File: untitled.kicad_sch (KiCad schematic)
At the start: 0 parts

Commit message: updated DacSheet
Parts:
- added IC1: ES9023P, customfootprints:SOIC127P600X175-16N, symbol esp32lib:ES9023P
- added U14: NAU88C22YG, customfootprints:nau88c22, symbol modcaneuro:NAU88C22YG

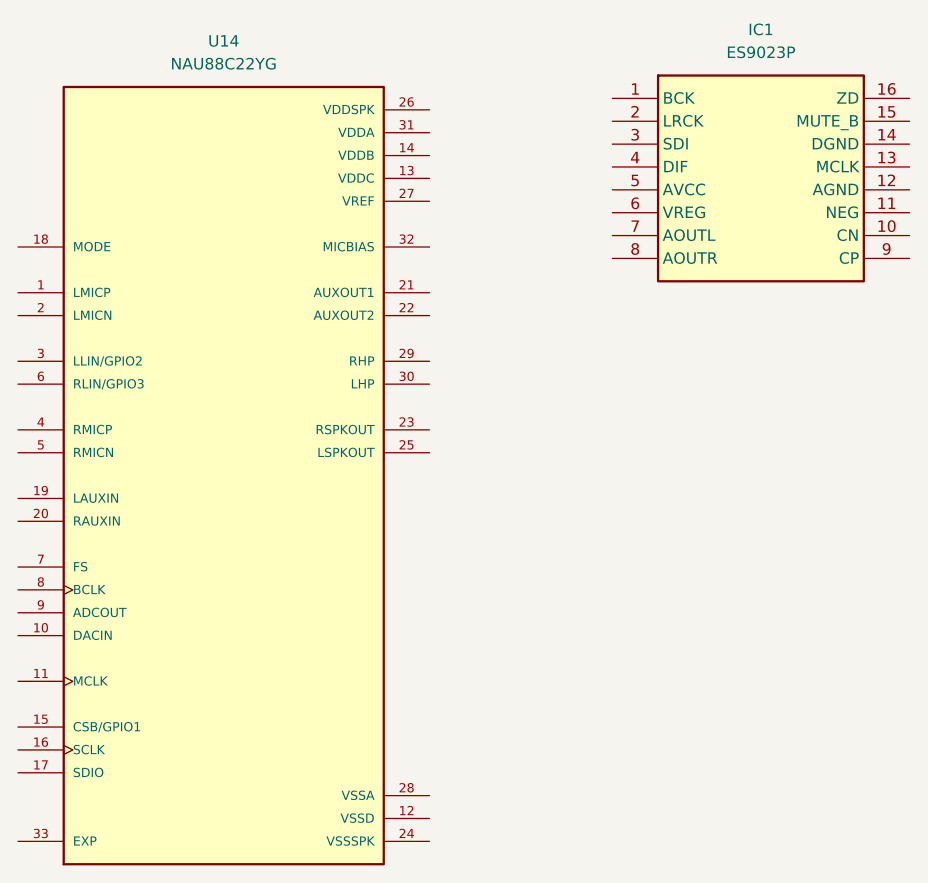
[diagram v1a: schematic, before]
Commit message: added codec
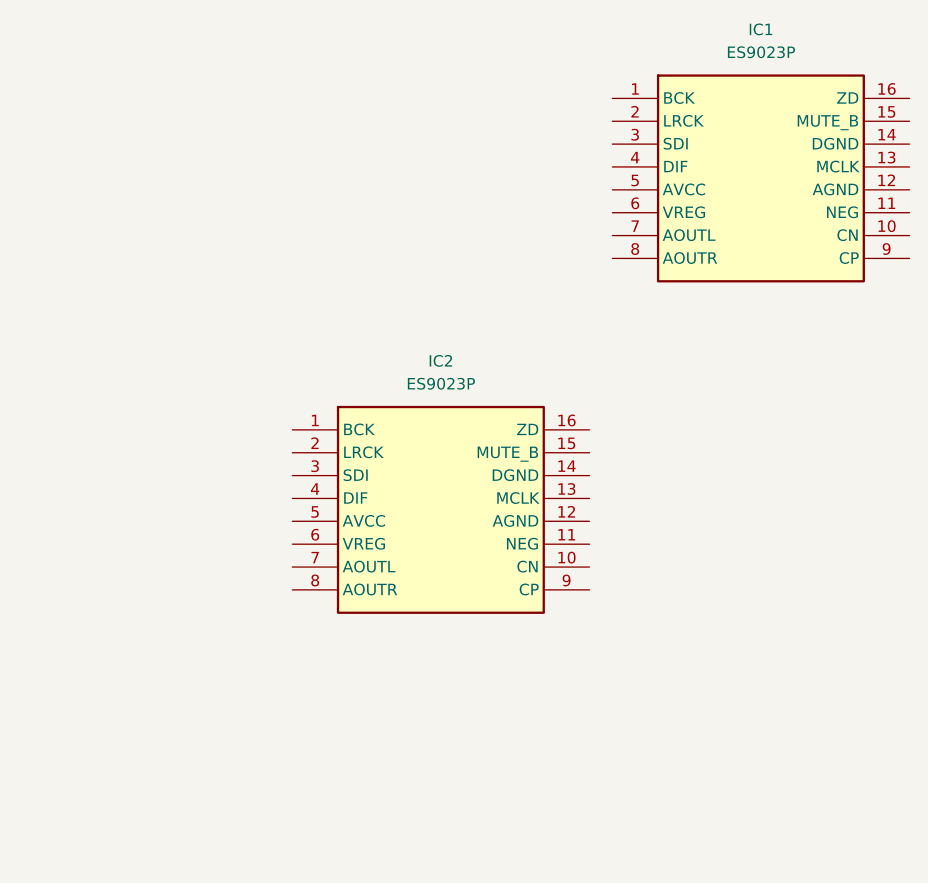
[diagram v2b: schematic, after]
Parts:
- removed U14: NAU88C22YG, customfootprints:nau88c22, symbol modcaneuro:NAU88C22YG
- added IC2: ES9023P, customfootprints:SOIC127P600X175-16N, symbol esp32lib:ES9023P
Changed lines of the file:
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@@
 	)
 	(symbol
-		(lib_id "modcaneuro:NAU88C22YG")
-		(at 163.83 77.47 0)
+		(lib_id "esp32lib:ES9023P")
+		(at 171.45 72.39 0)
 		(unit 1)
 		(exclude_from_sim no)
@@
 		(dnp no)
 		(fields_autoplaced yes)
-		(property "Reference" "U14"
-			(at 163.83 29.21 0)
+		(property "Reference" "IC2"
+			(at 187.96 64.77 0)
 			(effects
 				(font
@@
 			)
 		)
-		(property "Value" "NAU88C22YG"
-			(at 163.83 31.75 0)
+		(property "Value" "ES9023P"
+			(at 187.96 67.31 0)
 			(effects
 				(font
@@
 			)
 		)
-		(property "Footprint" "customfootprints:nau88c22"
-			(at 163.83 77.47 0)
+		(property "Footprint" "customfootprints:SOIC127P600X175-16N"
+			(at 200.66 167.31 0)
 			(effects
 				(font
 					(size 1.27 1.27)
 				)
-				(justify bottom)
+				(justify left top)
 				(hide yes)
 			)
 		)
 		(property "Datasheet" ""
-			(at 163.83 77.47 0)
+			(at 200.66 267.31 0)
+			(effects
+				(font
+					(size 1.27 1.27)
+				)
+				(justify left top)
+				(hide yes)
+			)
+		)
+		(property "Description" "Audio D/A Converter ICs Sabre 2V RMS stereo DAC"
+			(at 171.45 72.39 0)
 			(effects
 				(font
@@
 			)
 		)
-		(property "Description" ""
-			(at 163.83 77.47 0)
+		(property "Height" "1.75"
+			(at 200.66 467.31 0)
 			(effects
 				(font
 					(size 1.27 1.27)
 				)
+				(justify left top)
 				(hide yes)
 			)
 		)
-		(property "PARTREV" "3.3"
-			(at 163.83 77.47 0)
+		(property "Mouser Part Number" "460-ES9023P"
+			(at 200.66 567.31 0)
 			(effects
 				(font
 					(size 1.27 1.27)
 				)
-				(justify bottom)
+				(justify left top)
 				(hide yes)
 			)
 		)
-		(property "STANDARD" "Manufacturer Recommendations"
-			(at 163.83 77.47 0)
+		(property "Mouser Price/Stock" "https://www.mouser.co.uk/ProductDetail/ESS-Technology/ES9023P?qs=sPbYRqrBIVn%252BcPkDS1h3%252BQ%3D%3D"
+			(at 200.66 667.31 0)
 			(effects
 				(font
 					(size 1.27 1.27)
 				)
-				(justify bottom)
+				(justify left top)
 				(hide yes)
 			)
 		)
-		(property "MAXIMUM_PACKAGE_HEIGHT" "0.80mm"
-			(at 163.83 77.47 0)
+		(property "Manufacturer_Name" "ESS Technology"
+			(at 200.66 767.31 0)
 			(effects
 				(font
 					(size 1.27 1.27)
 				)
-				(justify bottom)
+				(justify left top)
 				(hide yes)
 			)
 		)
-		(property "MANUFACTURER" "Nuvoton"
-			(at 163.83 77.47 0)
+		(property "Manufacturer_Part_Number" "ES9023P"
+			(at 200.66 867.31 0)
 			(effects
 				(font
 					(size 1.27 1.27)
 				)
-				(justify bottom)
+				(justify left top)
 				(hide yes)
 			)
 		)
+		(pin "9"
+		)
+		(pin "4"
+		)
+		(pin "2"
+		)
+		(pin "5"
+		)
+		(pin "10"
+		)
+		(pin "7"
+		)
+		(pin "15"
+		)
+		(pin "16"
+		)
+		(pin "6"
+		)
+		(pin "8"
+		)
 		(pin "13"
 		)
-		(pin "17"
-		)
-		(pin "31"
-		)
-		(pin "33"
-		)
-		(pin "12"
-		)
-		(pin "26"
-		)
-		(pin "20"
-		)
-		(pin "28"
-		)
-		(pin "4"
+		(pin "1"
 		)
 		(pin "14"
@@
 		(pin "11"
 		)
-		(pin "16"
-		)
-		(pin "23"
-		)
-		(pin "24"
-		)
-		(pin "1"
-		)
-		(pin "29"
-		)
-		(pin "27"
-		)
-		(pin "25"
-		)
-		(pin "19"
-		)
-		(pin "21"
-		)
-		(pin "8"
-		)
-		(pin "7"
-		)
-		(pin "10"
-		)
-		(pin "15"
-		)
-		(pin "5"
-		)
-		(pin "6"
-		)
-		(pin "22"
-		)
-		(pin "9"
-		)
-		(pin "2"
+		(pin "12"
 		)
 		(pin "3"
 		)
-		(pin "18"
-		)
-		(pin "30"
-		)
-		(pin "32"
-		)
 		(instances
-			(project ""
+			(project "esp32"
 				(path "/c4754426-a41b-4341-9d09-2e389619f3d6/a94728e7-5369-4898-bc9c-adaf2aafacfb/157057dc-edda-48cb-83c9-cb6b8a11bb6d"
-					(reference "U14")
+					(reference "IC2")
 					(unit 1)
 				)
